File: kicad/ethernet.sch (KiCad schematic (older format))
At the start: 46 parts, among them J5 L829-1J1T-43, U5 10CL025ZE144, U6 KSZ9021GN

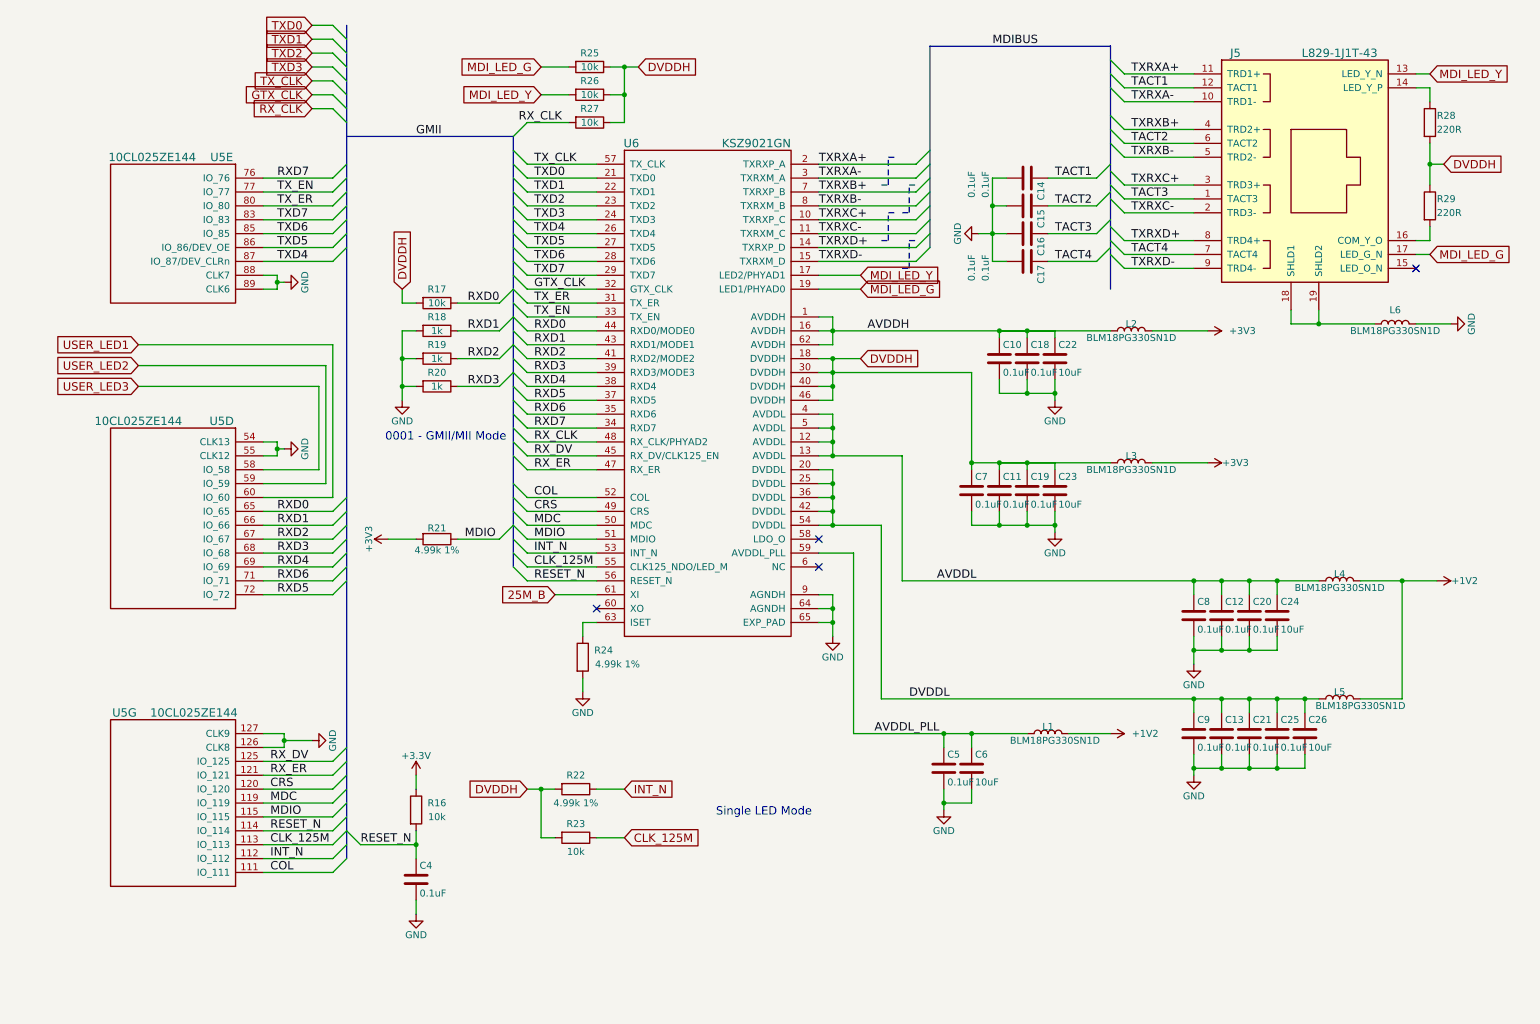
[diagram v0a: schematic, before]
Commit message: Removed footprint for unused components Updated 3d model for LQFP-144 Updated symbol library Updated schematics Updated PCB - finished routing
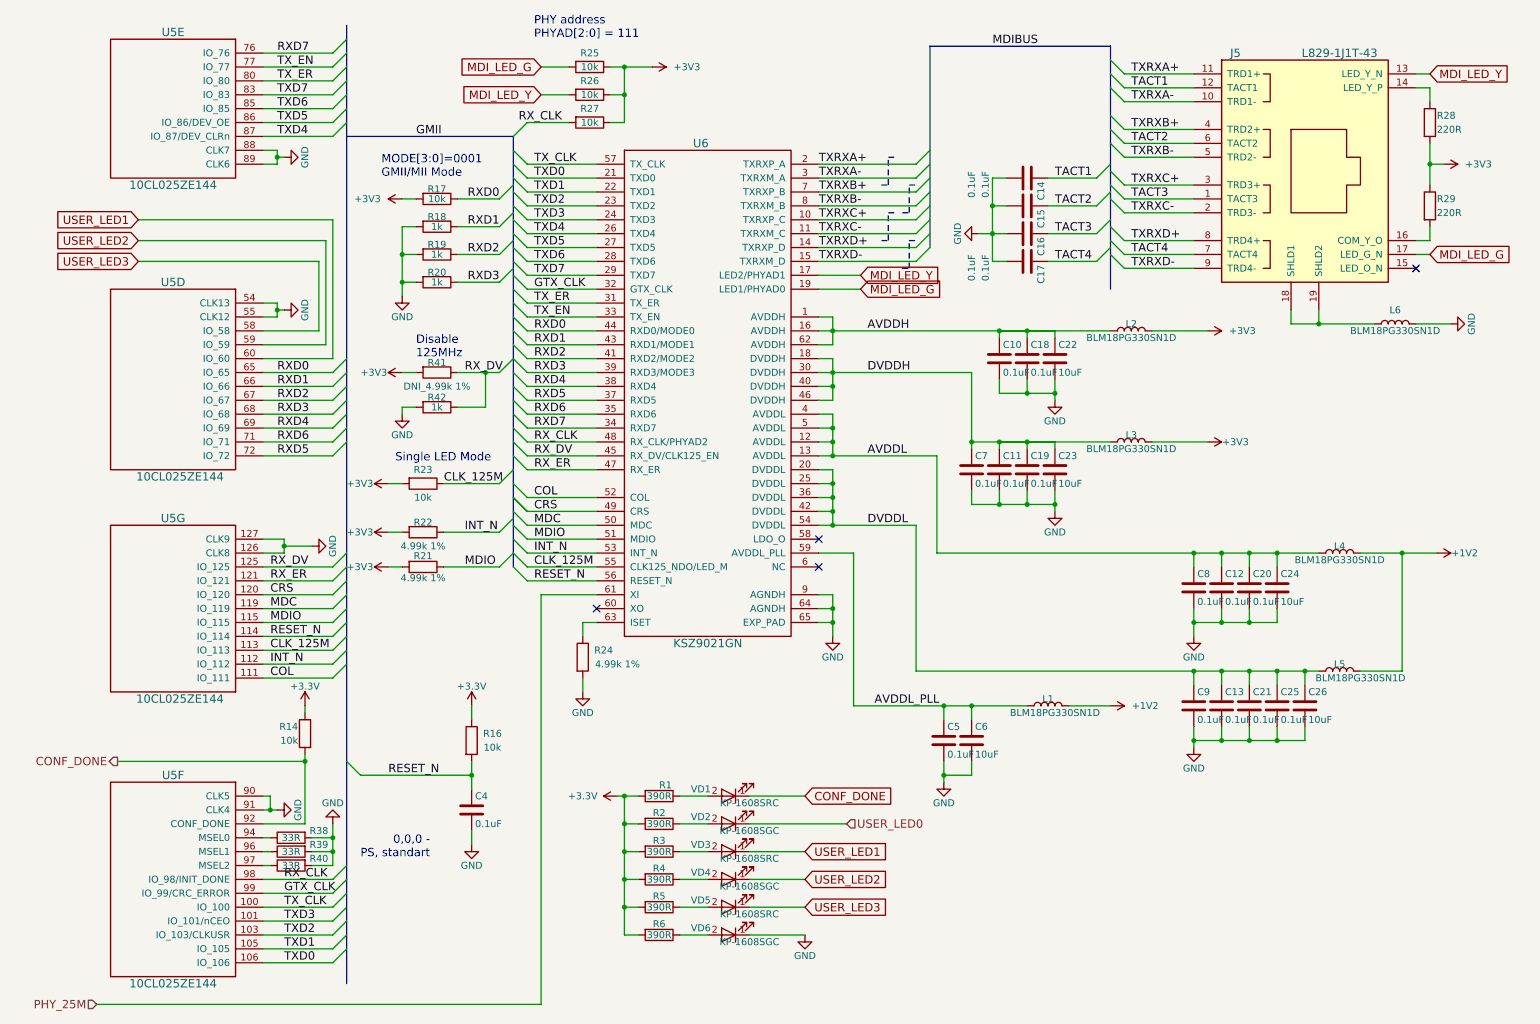
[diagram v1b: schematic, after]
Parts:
- added R1, R2, R3, R4, R5, R6: 390R, Resistors_SMD:R_0603, symbol R
- added R14: 10k, Resistors_SMD:R_0603, symbol R
- added R38, R39, R40: 33R, Resistors_SMD:R_0603, symbol R
- added R41: DNI_4.99k 1%, Resistors_SMD:R_0603, symbol R
- added R42: 1k, Resistors_SMD:R_0603, symbol R
- added unit 6 of U5
- added VD1, VD3, VD5: KP-1608SRC, LEDs:LED_0603, symbol LED
- added VD2, VD4, VD6: KP-1608SGC, LEDs:LED_0603, symbol LED
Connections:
- net +3V3: now also R17.2, R22.2, R23.2, R25.1, R26.1, R27.1, R28.2, R29.1, R1.2, R14.1, R2.2, R3.2, R4.2, R41.2, R5.2, R6.2
- net DVDDH: no longer R17.2, R22.2, R23.2, R25.1, R26.1, R27.1, R28.2, R29.1
- net GND: now also R38.2, R39.2, R40.2, R42.2, U5.90 (CLK5), U5.91 (CLK4), VD6.1 (K)
- net GTX_CLK: now also U5.99 (IO_99/CRC_ERROR)
- net RX_CLK: now also U5.98 (IO_98/INIT_DONE)
- net RX_DV: now also R41.1, R42.1
- net TXD0: now also U5.106 (IO_106)
- net TXD1: now also U5.105 (IO_105)
- net TXD2: now also U5.103 (IO_103/CLKUSR)
- net TXD3: now also U5.101 (IO_101/nCEO)
- net TX_CLK: now also U5.100 (IO_100)
- net USER_LED1: now also VD3.1 (K)
- net USER_LED2: now also VD4.1 (K)
- net USER_LED3: now also VD5.1 (K)
- net 25M_B renamed PHY_25M
- new net: R38.1, U5.94 (MSEL0)
- new net: R39.1, U5.96 (MSEL1)
- new net: R40.1, U5.97 (MSEL2)
- new net: R2.1, VD2.2 (A)
- new net: R6.1, VD6.2 (A)
- new net: R3.1, VD3.2 (A)
- new net: R1.1, VD1.2 (A)
- new net: R4.1, VD4.2 (A)
- new net: R5.1, VD5.2 (A)
- new net CONF_DONE: R14.2, U5.92 (CONF_DONE), VD1.1 (K)
- new net USER_LED0: VD2.1 (K)
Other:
- note added: "0,0,0 - \nPS, standart"
- note added: "Disable \n125MHz"
- note added: "MODE[3:0]=0001\nGMII/MII Mode"
- note added: "PHY address\nPHYAD[2:0] = 111\n"
- note removed: "0001 - GMII/MII Mode"
- moved on the sheet: C11, C12, C13, C19, C20, C21, C23, C24, C25, C26, C4, C5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

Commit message: Updated footprint and 3D model for ksz9021gn (it was wrong)
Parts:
- U6: footprint Housings_DFN_QFN:QFN-64-1EP_9x9mm_Pitch0.5mm -> library:QFN-64-1EP_8x8mm_Pitch0.4mm
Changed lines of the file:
@@
 F 0 "U6" H 5350 4750 60  0000 C CNN
 F 1 "KSZ9021GN" H 5400 1150 60  0000 C CNN
-F 2 "Housings_DFN_QFN:QFN-64-1EP_9x9mm_Pitch0.5mm" H 5150 4000 60  0001 C CNN
+F 2 "library:QFN-64-1EP_8x8mm_Pitch0.4mm" H 5150 4000 60  0001 C CNN
 F 3 "" H 5150 4000 60  0001 C CNN
 F 4 "KSZ9021GN" H 5400 3100 60  0001 C CNN "MFPN"

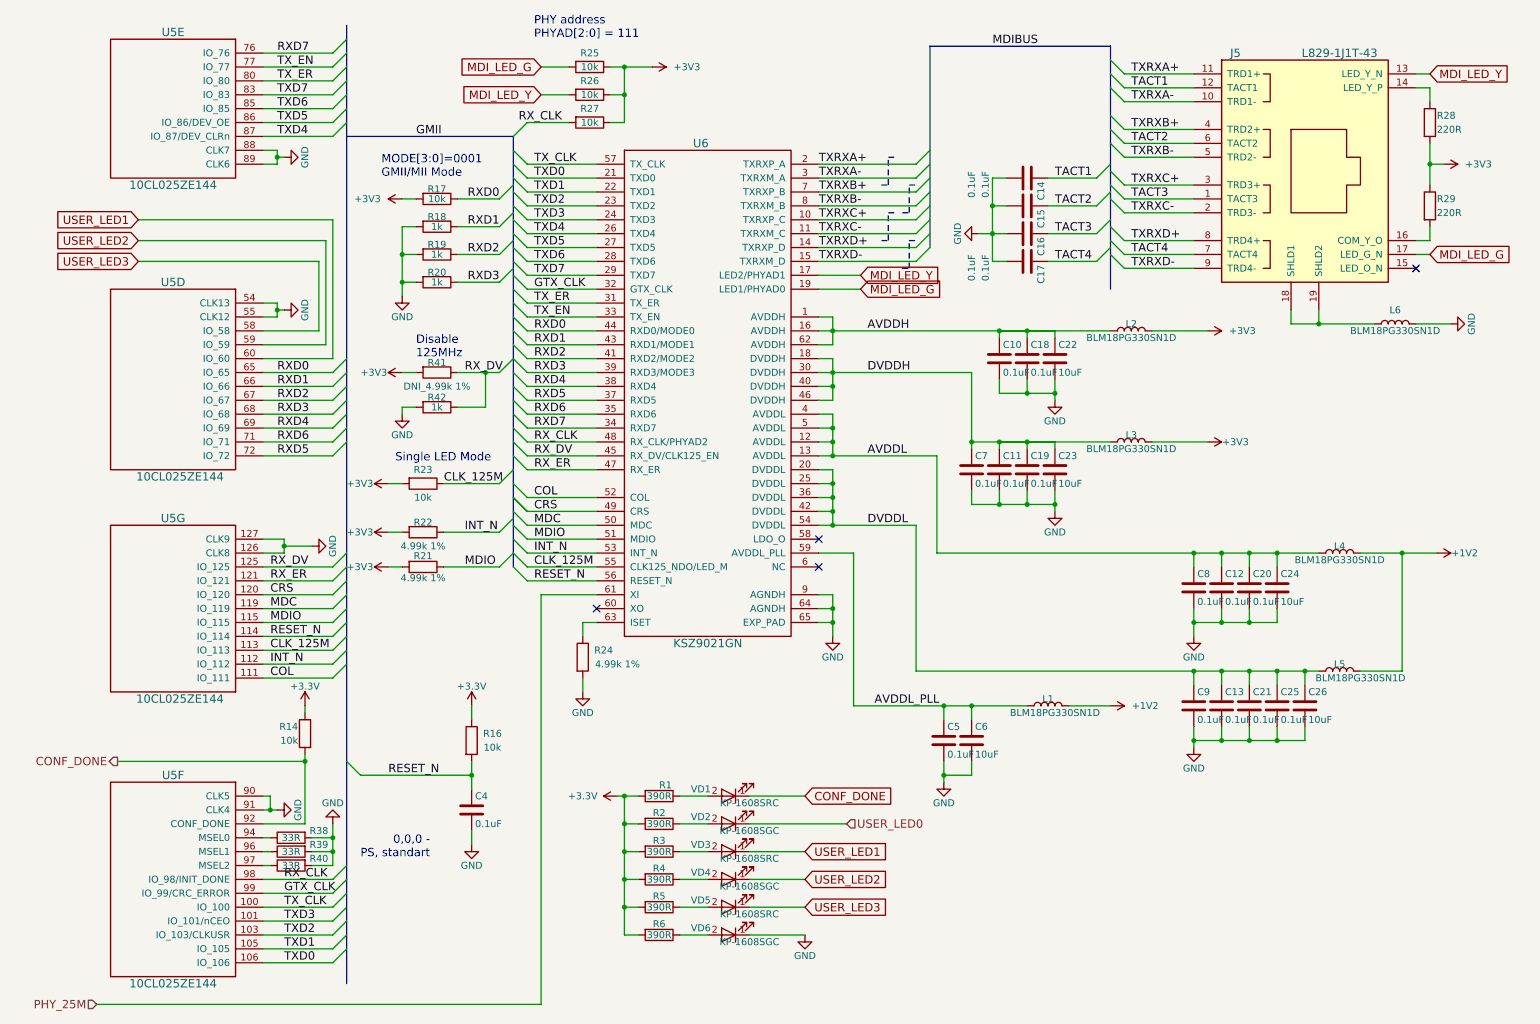
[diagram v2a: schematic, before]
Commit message: Add datasheets for new components (Leds, Button, TestPoint) Add 3D models for new components (Leds, Button, TestPoint) Add footprints for new components (Leds, Button, TestPoint) Add new components to schematic library.
Schematic changes:
Change revision 1.0 -> 2.0
Add dual-color and RGB leds. Connect to FPGA.
Add tespoint for GND connection.
Add 2 tactile smd button. Connect to FPGA.
Remove User Gpio Header.
Reconnect FPGA-to-Raspberry connections

PCB changes:
Change revision 1.0 -> 2.0
Rotate RJ-45 connector
Remove text REF around fidusial.
Place new components (Leds, Button, TestPoint)
All connections routed
DRC ok (one error for fidusial)
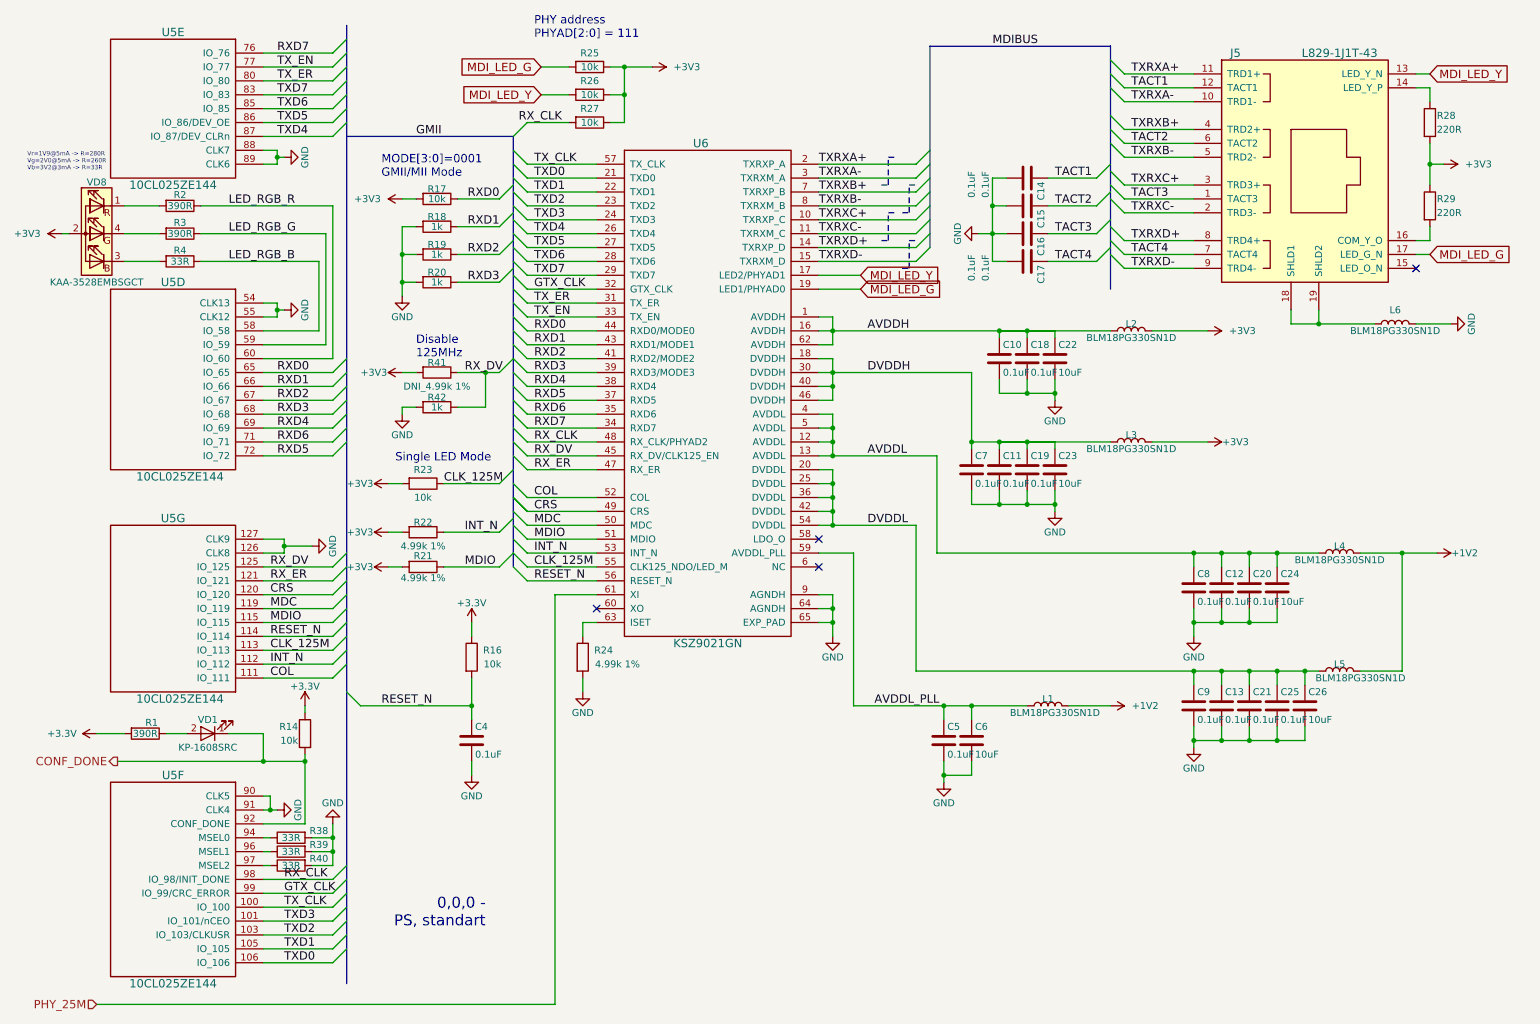
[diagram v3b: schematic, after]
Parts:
- removed R5, R6: 390R, Resistors_SMD:R_0603, symbol R
- removed VD2, VD4, VD6: KP-1608SGC, LEDs:LED_0603, symbol LED
- removed VD3, VD5: KP-1608SRC, LEDs:LED_0603, symbol LED
- added VD8: KAA-3528EMBSGCT, project_footprints:LED_RGB_3528, symbol LED_RABG
- R4: value 390R -> 33R; DESC RES SMD 390R OHM 1% 1/10W 0603 -> RES SMD 33R OHM 1% 1/10W 0603; MFPN RC0603FR-07390RL -> RC0603FR-0733RL
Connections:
- net USER_LED1 is gone; now on net LED_RGB_R: U5.60 (IO_60)
- net USER_LED2 is gone; now on net LED_RGB_G: U5.59 (IO_59)
- net USER_LED3 is gone; now on net LED_RGB_B: U5.58 (IO_58)
- net +3V3: now also VD8.2 (A); no longer R2.2, R3.2, R4.2
- net LED_RGB_R: now reaches R2.1
- net LED_RGB_G: now reaches R3.1
- net LED_RGB_B: now reaches R4.1
- new net: R2.2, VD8.1 (RK)
- new net: R3.2, VD8.4 (GK)
- new net: R4.2, VD8.3 (BK)
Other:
- note added: "Vr=1V9@5mA -> R=280R\nVg=2V0@5mA -> R=260R\nVb=3V2@3mA -> R=33R"
- moved on the sheet: C4, R1, R16, R2, R3, VD1
